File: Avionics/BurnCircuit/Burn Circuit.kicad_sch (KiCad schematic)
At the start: 12 parts, among them Q1 NPN, U1 PE014006

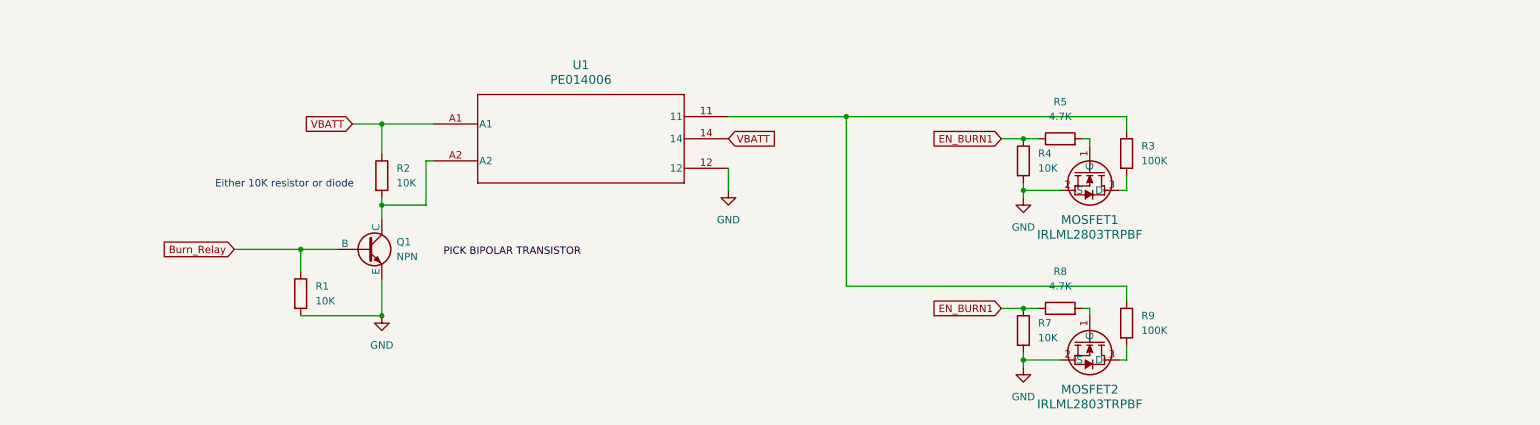
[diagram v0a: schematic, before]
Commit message: need to add net classes
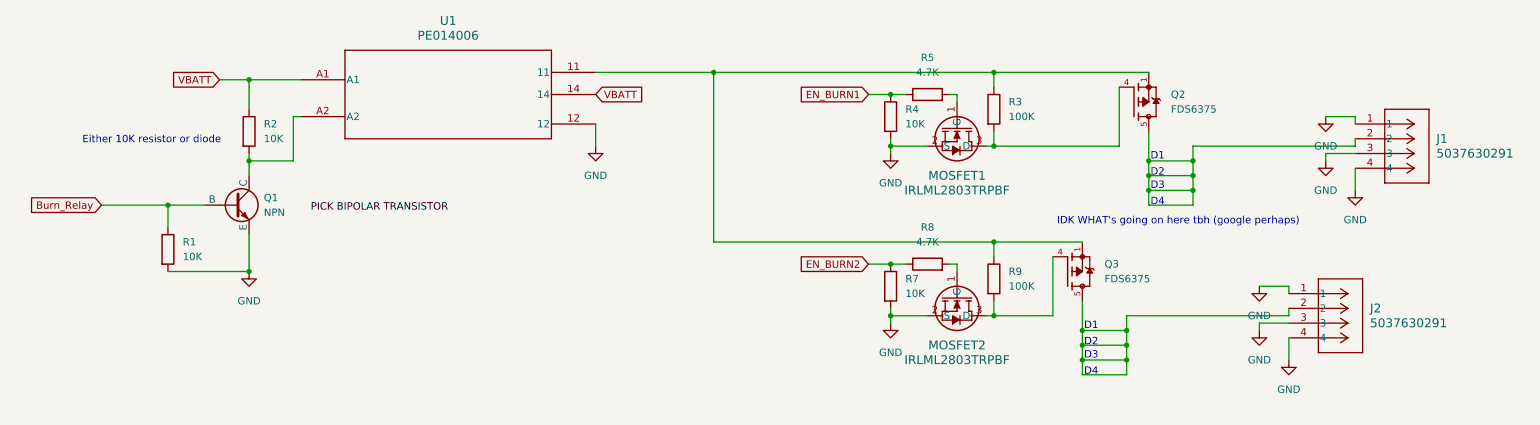
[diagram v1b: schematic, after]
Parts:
- added J1, J2: 5037630291, 5037630291:CON_5037630291, symbol 5037630291:5037630291
- added Q2, Q3: FDS6375, FDS6375 (1):SOIC127P600X175-8N, symbol FDS6375:FDS6375
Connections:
- net EN_BURN1: no longer R7.1, R8.1
- net GND: now also J1.1, J1.3, J1.4, J2.1, J2.3, J2.4
- net at MOSFET2.3 (D), R9.2: now also Q3.4
- net at R3.1, R9.1, U1.11: now also Q2.1, Q3.1
- net at MOSFET1.3 (D), R3.2: now also Q2.4
- new net: J2.2, Q3.5
- new net: J1.2, Q2.5
- new net EN_BURN2: R7.1, R8.1
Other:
- note added: "D1"
- note added: "D2"
- note added: "D3"
- note added: "D4"
- note added: "IDK WHAT's going on here tbh (google perhaps)"
- moved on the sheet: MOSFET1, MOSFET2, Q1, R1, R2, R3, R4, R5, R7, R8, R9, U1
